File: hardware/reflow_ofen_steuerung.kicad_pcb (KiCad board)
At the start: 2 copper layers, 150.9 x 55.9 mm, 48 parts, among them J1 230VAC, J10 GND, J2 Heizung oben, J3 Heizung unten, J4 AVR-ISP-6, J5 LCD Display, J6 Encoder, J7 FAN, J8 +5V, J9 +12V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

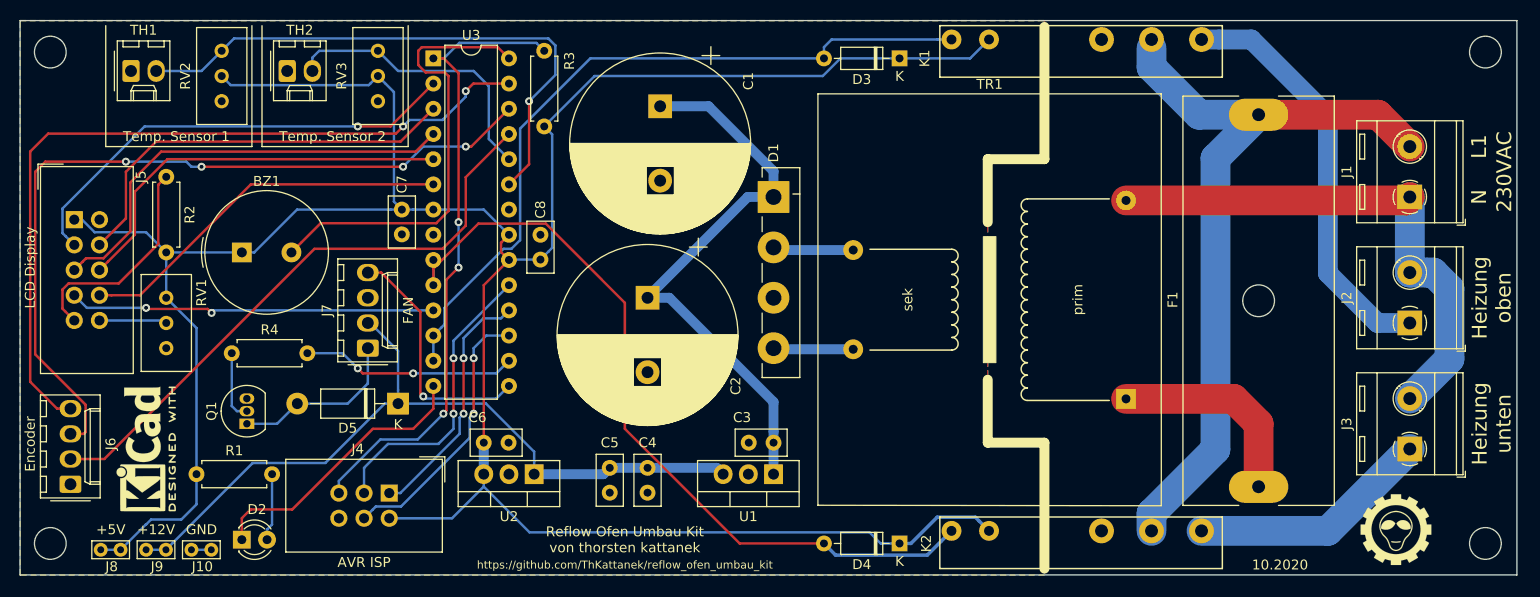
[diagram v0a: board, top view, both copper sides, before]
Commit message: PCB angepasst für Kühlkörper der Spannungsregler
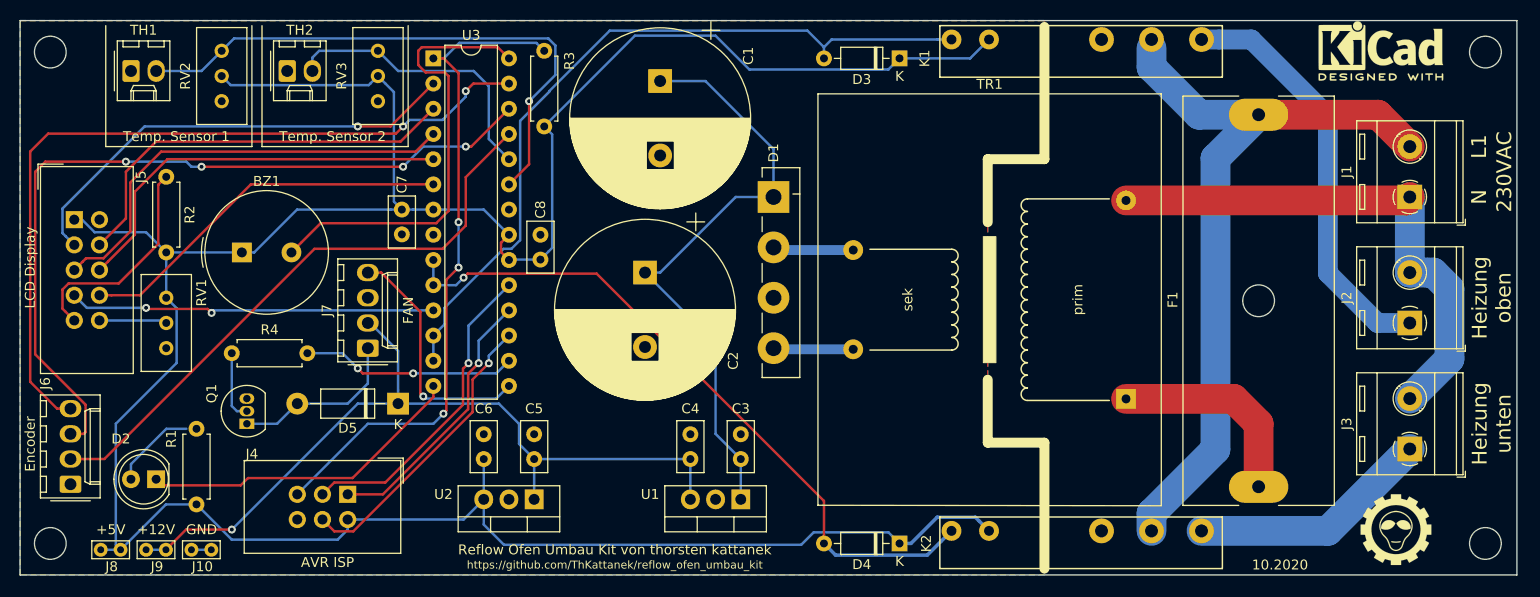
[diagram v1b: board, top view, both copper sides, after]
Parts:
- D2: footprint LED_THT:LED_D3.0mm -> LED_THT:LED_D5.0mm
- moved REF** 130.8 mm to (189.5, 51.3), turned to 0 degrees
- moved D2 10.6 mm to (66.0, 94.5), turned to 180 degrees
- moved C5 7.67 mm to (104.1, 92.5), turned to 90 degrees
- moved C4 4.41 mm to (119.9, 92.5), turned to 90 degrees
- moved J4 4.19 mm to (85.3, 96.0)
- moved U1 4.17 mm to (125.0, 96.5)
- moved C3 3.69 mm to (125.0, 92.5), turned to 90 degrees
- moved R1 3.05 mm to (70.1, 97.0), turned to 90 degrees
- moved C2 2.55 mm to (115.3, 73.7)
- moved C1 2.54 mm to (116.8, 54.4)
- moved U2 2.54 mm to (104.1, 96.5)
- moved C6 1.65 mm to (99.1, 92.5), turned to 90 degrees
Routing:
- net +5V: track 276.0 -> 289.6 mm
- net HEIZUNG_UNTEN: track 80.6 -> 70.5 mm, vias 0 -> 1
- net Net-(D2-Pad1): track 28.3 -> 33.0 mm
- net Net-(C1-Pad1): track 58.0 -> 62.1 mm
- net +12V: track 78.6 -> 82.1 mm, vias 0 -> 1
- net RST: track 64.8 -> 68.4 mm
- net MOSI: track 27.3 -> 29.8 mm, vias 2 -> 1
- net HEIZUNG_OBEN: track 75.4 -> 77.7 mm
- net MISO: track 25.1 -> 27.4 mm, vias 2 -> 1
- net SCK: track 30.0 -> 31.9 mm, vias 2 -> 1
- net Net-(D2-Pad2): track 6.81 -> 8.58 mm

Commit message: added 150 ohm resistor for buzzer
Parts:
- added R5: 150, Resistor_THT:R_Axial_DIN0207_L6.3mm_D2.5mm_P7.62mm_Horizontal, F.Cu at (73.7, 76.2)
- C3, C5: value 330n -> 0,33u; footprint Capacitor_THT:C_Disc_D5.0mm_W2.5mm_P2.50mm -> Capacitor_THT:CP_Radial_D4.0mm_P1.50mm
- moved BZ1 4.19 mm to (75.7, 67.6)
- turned C3 to 180 degrees
- turned C5 to 180 degrees
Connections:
- BZ1 pad 1: +5V -> Net-(BZ1-Pad1)
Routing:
- net GND: track 2.00 -> 12.1 mm, vias 0 -> 1
- net Net-(BZ1-Pad1): track 0.00 -> 9.48 mm
- net +5V: track 289.6 -> 295.1 mm
- net BUZZER: track 45.9 -> 44.1 mm
- net Net-(D2-Pad2): track 8.58 -> 9.60 mm
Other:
- board text added: "Rev.: 1.0.0"
